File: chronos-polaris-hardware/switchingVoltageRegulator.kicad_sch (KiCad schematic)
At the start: 10 parts, among them U1 TLV62130RGTR

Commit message: asdf
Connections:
- net unknown1 renamed BAT+
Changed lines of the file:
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@@
 		)
 	)
-	(hierarchical_label "unknown1"
+	(hierarchical_label "BAT+"
 		(shape input)
 		(at 88.9 72.39 0)

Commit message: made satvik fixes
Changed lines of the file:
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@@
 	(wire
 		(pts
-			(xy 158.75 105.41) (xy 161.29 105.41)
+			(xy 158.75 105.41) (xy 163.83 105.41)
 		)
 		(stroke
@@
 	(wire
 		(pts
+			(xy 124.46 60.96) (xy 134.62 60.96)
+		)
+		(stroke
+			(width 0)
+			(type default)
+		)
+	)
+	(wire
+		(pts
 			(xy 88.9 72.39) (xy 88.9 92.71)
 		)
@@
 	(wire
 		(pts
+			(xy 135.89 77.47) (xy 135.89 80.01)
+		)
+		(stroke
+			(width 0)
+			(type default)
+		)
+	)
+	(wire
+		(pts
 			(xy 143.51 60.96) (xy 143.51 80.01)
 		)
@@
 		)
 	)
-	(global_label "5V"
+	(hierarchical_label "5V"
 		(shape input)
-		(at 134.62 60.96 180)
+		(at 163.83 105.41 0)
+		(fields_autoplaced yes)
+		(effects
+			(font
+				(size 1.27 1.27)
+			)
+			(justify left)
+		)
+	)
+	(hierarchical_label "BAT+"
+		(shape input)
+		(at 88.9 72.39 0)
+		(fields_autoplaced yes)
+		(effects
+			(font
+				(size 1.27 1.27)
+			)
+			(justify left)
+		)
+	)
+	(hierarchical_label "5V"
+		(shape input)
+		(at 124.46 60.96 180)
 		(fields_autoplaced yes)
 		(effects
@@
 			(justify right)
 		)
-		(property "Intersheetrefs" "${INTERSHEET_REFS}"
-			(at 129.4161 60.96 0)
-			(effects
-				(font
-					(size 1.27 1.27)
-				)
-				(justify right)
-				(hide yes)
-			)
-		)
-	)
-	(global_label "5V_5%BOOST"
+	)
+	(hierarchical_label "5V_5%BOOST"
 		(shape input)
-		(at 135.89 80.01 90)
+		(at 135.89 77.47 90)
 		(fields_autoplaced yes)
 		(effects
-			(font
-				(size 1.27 1.27)
-			)
-			(justify left)
-		)
-		(property "Intersheetrefs" "${INTERSHEET_REFS}"
-			(at 135.89 65.0695 90)
-			(effects
-				(font
-					(size 1.27 1.27)
-				)
-				(justify left)
-				(hide yes)
-			)
-		)
-	)
-	(global_label "5V"
-		(shape input)
-		(at 161.29 105.41 0)
-		(fields_autoplaced yes)
-		(effects
-			(font
-				(size 1.27 1.27)
-			)
-			(justify left)
-		)
-		(property "Intersheetrefs" "${INTERSHEET_REFS}"
-			(at 166.4939 105.41 0)
-			(effects
-				(font
-					(size 1.27 1.27)
-				)
-				(justify left)
-				(hide yes)
-			)
-		)
-	)
-	(hierarchical_label "BAT+"
-		(shape input)
-		(at 88.9 72.39 0)
-		(fields_autoplaced yes)
-		(effects

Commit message: clean up
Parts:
- added C11: 22uF, Capacitor_SMD:C_0603_1608Metric, symbol Device:C
- added C12: 4.7uF, Capacitor_SMD:C_0805_2012Metric, symbol Device:C
- added L2: 2.2uH, polaris-fp:IND-SMD_L4.0-W4.0, symbol Device:L
- added R2: 240k, Resistor_SMD:R_0603_1608Metric, symbol Device:R
- added R3: 27.4k, Resistor_SMD:R_0603_1608Metric, symbol Device:R
- added U6: TPS629206DRLR, SOT5X3-8_DRL_TEX, symbol 2024-10-27_20-41-39:TPS629206DRLR
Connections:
- net 5V: now also C11.2, L2.1, U6.3 (VOS)
- net GND: now also C11.1, C12.2, R2.1, R3.2, U6.5 (GND)
- new net: R2.2, U6.1 (FB/VSET)
- new net: L2.2, U6.4 (SW)
- new net: C12.1, U6.6 (VIN), U6.7 (EN)
- new net: R3.1, U6.8 (MODE/S-CONF)
- no-connect marks 0 -> 1
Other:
- moved on the sheet: L1

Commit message: Fixed warnings and error messages. - Rishik B.
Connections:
- net VIN: now reaches C12.1, U6.6 (VIN), U6.7 (EN)

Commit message: end it all
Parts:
- U6: footprint SOT5X3-8_DRL_TEX -> footprints:SOT5X3-8_DRL_TEX
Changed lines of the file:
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@@
 			)
 		)
-		(property "Footprint" "SOT5X3-8_DRL_TEX"
+		(property "Footprint" "footprints:SOT5X3-8_DRL_TEX"
 			(at 67.31 138.43 0)
 			(effects

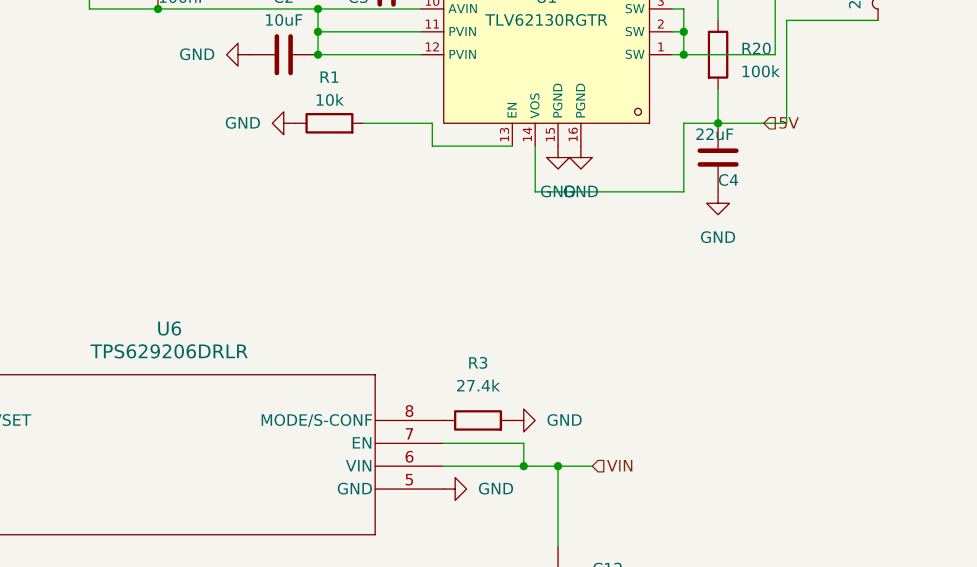
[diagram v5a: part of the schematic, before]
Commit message: Schematic Changes as per DR1 Suggestions
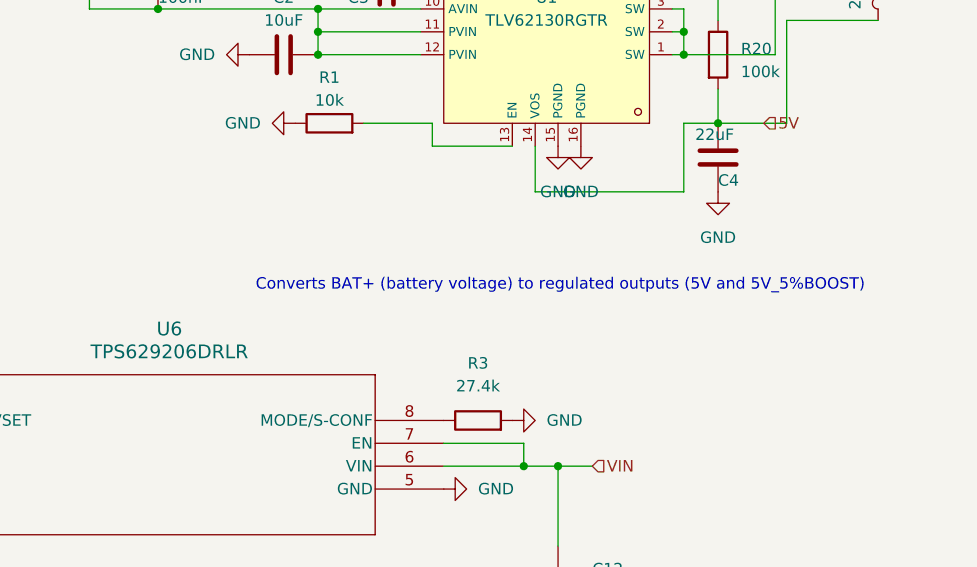
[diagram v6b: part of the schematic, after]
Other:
- note added: "Converts BAT+ (battery voltage) to regulated outputs (5V and 5V_5%BOOST)"
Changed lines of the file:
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@@
+		)
+	)
+	(text "Converts BAT+ (battery voltage) to regulated outputs (5V and 5V_5%BOOST)"
+		(exclude_from_sim no)
+		(at 141.224 123.444 0)
+		(effects
+			(font
+				(size 1.27 1.27)
+			)
 		)
 	)
@@
 			)
 		)
-		(property "Datasheet" "TPS629206DRLR"
+		(property "Datasheet" "https://www.ti.com/lit/ds/symlink/tps629206.pdf?ts=1740282913128&ref_url=https%253A%252F%252Fwww.mouser.com%252F"
 			(at 67.31 138.43 0)
 			(effects
